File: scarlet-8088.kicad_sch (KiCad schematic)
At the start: 0 parts

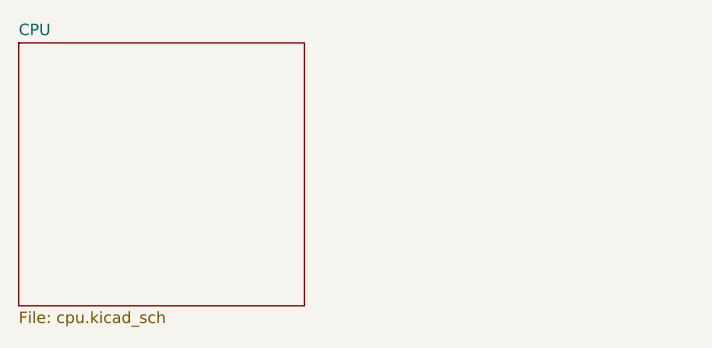
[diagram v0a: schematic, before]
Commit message: cpu and fpu connected together
Signed-off-by: Lucy Mielke <user@domain.tld>
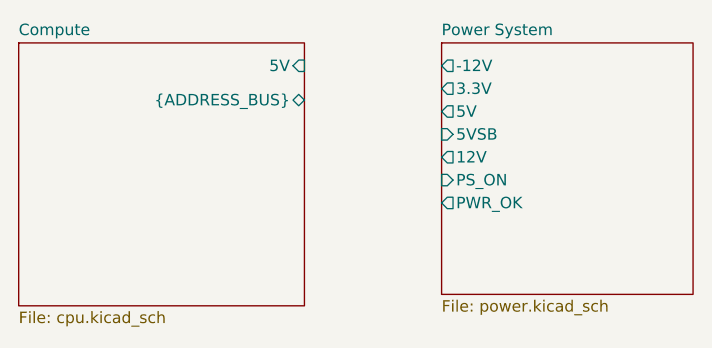
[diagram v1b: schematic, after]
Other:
- sheet CPU renamed Compute
- added sheet Power System (power.kicad_sch)
- sheet Compute ports: added 5V, {ADDRESS_BUS}; removed none
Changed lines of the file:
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@@
+	)
+	(sheet
+		(at 101.6 58.42)
+		(size 27.94 27.94)
+		(exclude_from_sim no)
+		(in_bom yes)
+		(on_board yes)
+		(dnp no)
+		(fields_autoplaced yes)
+		(stroke
+			(width 0.1524)
+			(type solid)
+		)
+		(fill
+			(color 0 0 0 0)
+		)
+		(property "Sheetname" "Power System"
+			(at 101.6 57.7084 0)
+			(show_name no)
+			(do_not_autoplace no)
+			(effects
+				(font
+					(size 1.27 1.27)
+				)
+				(justify left bottom)
+			)
+		)
+		(property "Sheetfile" "power.kicad_sch"
+			(at 101.6 86.9446 0)
+			(show_name no)
+			(do_not_autoplace no)
+			(effects
+				(font
+					(size 1.27 1.27)
+				)
+				(justify left top)
+			)
+		)
+		(pin "-12V" output
+			(at 101.6 60.96 180)
+			(effects
+				(font
+					(size 1.27 1.27)
+				)
+				(justify left)
+			)
+		)
+		(pin "3.3V" output
+			(at 101.6 63.5 180)
+			(effects
+				(font
+					(size 1.27 1.27)
+				)
+				(justify left)
+			)
+		)
+		(pin "5V" output
+			(at 101.6 66.04 180)
+			(effects
+				(font
+					(size 1.27 1.27)
+				)
+				(justify left)
+			)
+		)
+		(pin "5VSB" input
+			(at 101.6 68.58 180)
+			(effects
+				(font
+					(size 1.27 1.27)
+				)
+				(justify left)
+			)
+		)
+		(pin "12V" output
+			(at 101.6 71.12 180)
+			(effects
+				(font
+					(size 1.27 1.27)
+				)
+				(justify left)
+			)
+		)
+		(pin "PS_ON" input
+			(at 101.6 73.66 180)
+			(effects
+				(font
+					(size 1.27 1.27)
+				)
+				(justify left)
+			)
+		)
+		(pin "PWR_OK" output
+			(at 101.6 76.2 180)
+			(effects
+				(font
+					(size 1.27 1.27)
+				)
+				(justify left)
+			)
+		)
+		(instances
+			(project "scarlet-8088"
+				(path "/6bf7a8bc-eb70-43f6-b16b-1b538dd0d96d"
+					(page "2")
+				)
+			)
+		)
 	)
 	(sheet
@@
 			(color 0 0 0 0)
 		)
-		(property "Sheetname" "CPU"
+		(property "Sheetname" "Compute"
 			(at 54.61 57.7084 0)
 			(show_name no)
@@
 			)
 		)
+		(pin "5V" input
+			(at 86.36 60.96 0)
+			(effects
+				(font
+					(size 1.27 1.27)
+				)
+				(justify right)
+			)
+		)
+		(pin "{ADDRESS_BUS}" bidirectional
+			(at 86.36 64.77 0)
+			(effects
+				(font
+					(size 1.27 1.27)
+				)
+				(justify right)
+			)
+		)
 		(instances
 			(project "scarlet-8088"
 				(path "/6bf7a8bc-eb70-43f6-b16b-1b538dd0d96d"
-					(page "2")
+					(page "3")
 				)
 			)

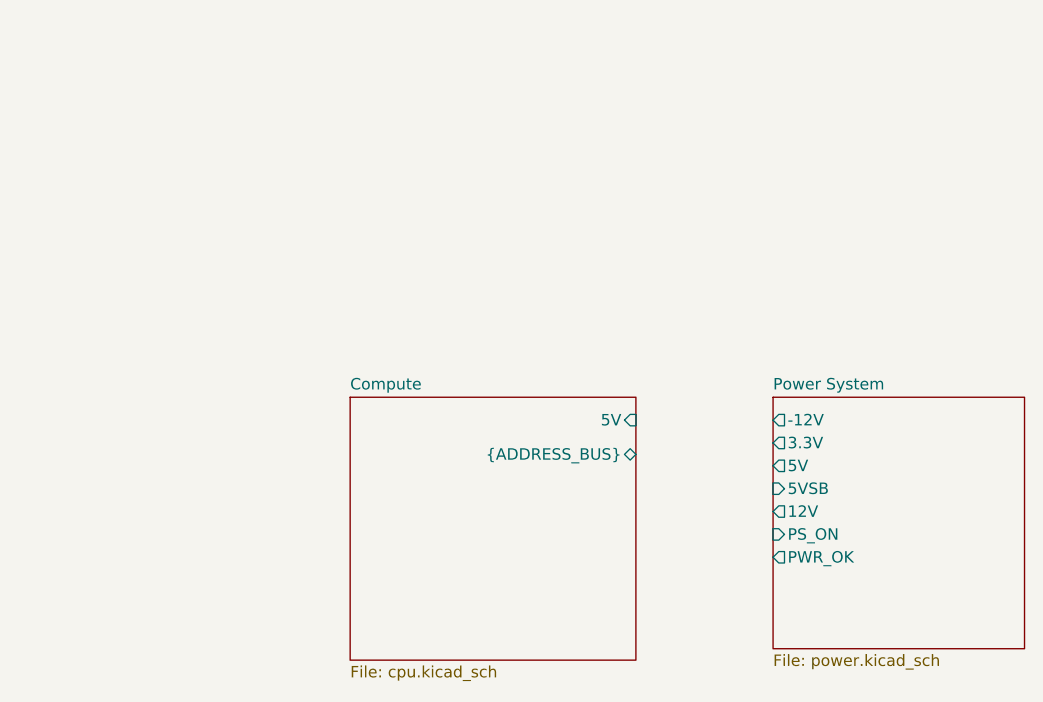
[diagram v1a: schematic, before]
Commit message: power delivery to compute basics
Signed-off-by: Lucy Mielke <user@domain.tld>
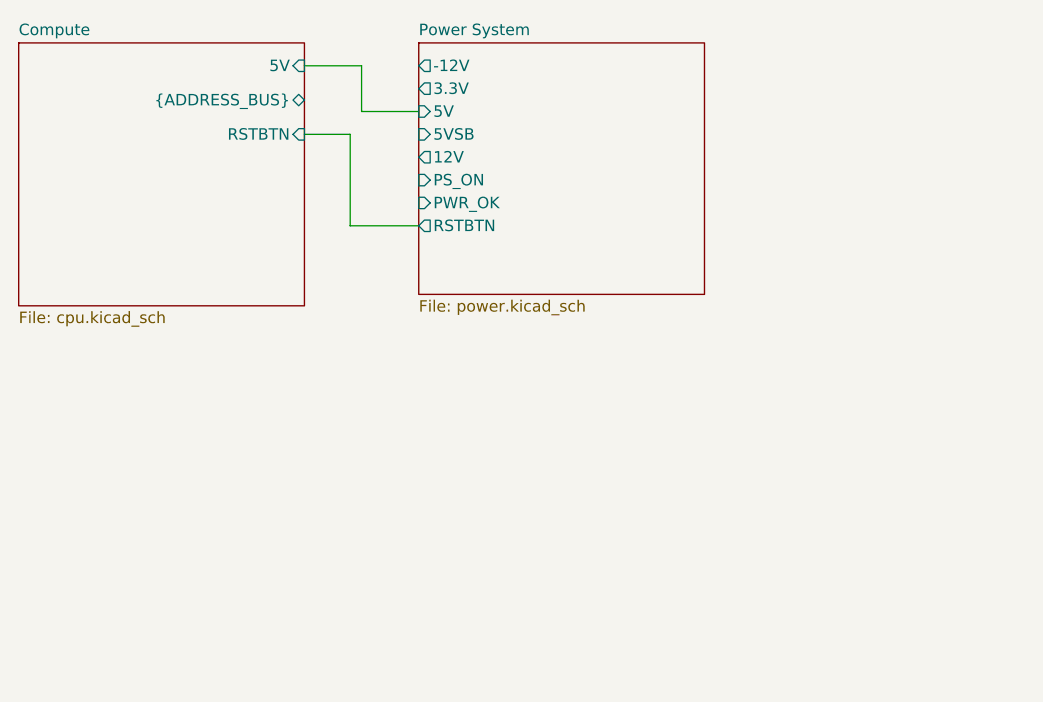
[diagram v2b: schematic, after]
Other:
- sheet Compute ports: added RSTBTN; removed none
- sheet Power System ports: added RSTBTN; removed none
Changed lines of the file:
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@@
 		(comment 1 "${COMMENT1}")
 	)
+	(wire
+		(pts
+			(xy 62.23 39.37) (xy 54.61 39.37)
+		)
+		(stroke
+			(width 0)
+			(type default)
+		)
+	)
+	(wire
+		(pts
+			(xy 62.23 26.67) (xy 55.88 26.67)
+		)
+		(stroke
+			(width 0)
+			(type default)
+		)
+	)
+	(wire
+		(pts
+			(xy 55.88 26.67) (xy 55.88 21.59)
+		)
+		(stroke
+			(width 0)
+			(type default)
+		)
+	)
+	(wire
+		(pts
+			(xy 54.61 29.21) (xy 49.53 29.21)
+		)
+		(stroke
+			(width 0)
+			(type default)
+		)
+	)
+	(wire
+		(pts
+			(xy 54.61 39.37) (xy 54.61 29.21)
+		)
+		(stroke
+			(width 0)
+			(type default)
+		)
+	)
+	(wire
+		(pts
+			(xy 55.88 21.59) (xy 49.53 21.59)
+		)
+		(stroke
+			(width 0)
+			(type default)
+		)
+	)
 	(sheet
-		(at 101.6 58.42)
-		(size 27.94 27.94)
+		(at 62.23 19.05)
+		(size 31.75 27.94)
 		(exclude_from_sim no)
 		(in_bom yes)
@@
 		)
 		(property "Sheetname" "Power System"
-			(at 101.6 57.7084 0)
+			(at 62.23 18.3384 0)
 			(show_name no)
 			(do_not_autoplace no)
@@
 		)
 		(property "Sheetfile" "power.kicad_sch"
-			(at 101.6 86.9446 0)
+			(at 62.23 47.5746 0)
 			(show_name no)
 			(do_not_autoplace no)
@@
 		)
 		(pin "-12V" output
-			(at 101.6 60.96 180)
+			(at 62.23 21.59 180)
 			(effects
 				(font
@@
 		)
 		(pin "3.3V" output
-			(at 101.6 63.5 180)
-			(effects
-				(font
-					(size 1.27 1.27)
-				)
-				(justify left)
-			)
-		)
-		(pin "5V" output
-			(at 101.6 66.04 180)
+			(at 62.23 24.13 180)
+			(effects
+				(font
+					(size 1.27 1.27)
+				)
+				(justify left)
+			)
+		)
+		(pin "5V" input
+			(at 62.23 26.67 180)
 			(effects
 				(font
@@
 		)
 		(pin "5VSB" input
-			(at 101.6 68.58 180)
+			(at 62.23 29.21 180)
 			(effects
 				(font
@@
 		)
 		(pin "12V" output
-			(at 101.6 71.12 180)
+			(at 62.23 31.75 180)
 			(effects
 				(font
@@
 		)
 		(pin "PS_ON" input
-			(at 101.6 73.66 180)
-			(effects
-				(font
-					(size 1.27 1.27)
-				)
-				(justify left)
-			)
-		)
-		(pin "PWR_OK" output
-			(at 101.6 76.2 180)
+			(at 62.23 34.29 180)
+			(effects
+				(font
+					(size 1.27 1.27)
+				)
+				(justify left)
+			)
+		)
+		(pin "PWR_OK" input
+			(at 62.23 36.83 180)
+			(effects
+				(font
+					(size 1.27 1.27)
+				)
+				(justify left)
+			)
+		)
+		(pin "RSTBTN" output
+			(at 62.23 39.37 180)
 			(effects
 				(font
@@
 	)
 	(sheet
-		(at 54.61 58.42)
+		(at 17.78 19.05)
 		(size 31.75 29.21)
 		(exclude_from_sim no)
@@
 		)
 		(property "Sheetname" "Compute"
-			(at 54.61 57.7084 0)
+			(at 17.78 18.3384 0)
 			(show_name no)
 			(do_not_autoplace no)
@@
 		)
 		(property "Sheetfile" "cpu.kicad_sch"
-			(at 54.61 88.2146 0)
+			(at 17.78 48.8446 0)
 			(show_name no)
 			(do_not_autoplace no)
@@
 		)
 		(pin "5V" input
-			(at 86.36 60.96 0)
+			(at 49.53 21.59 0)
 			(effects
 				(font
@@
 		)
 		(pin "{ADDRESS_BUS}" bidirectional
-			(at 86.36 64.77 0)
-			(effects
-				(font
+			(at 49.53 25.4 0)
+			(effects
+				(font
+					(size 1.27 1.27)
+				)
+				(justify right)
+			)
+		)
+		(pin "RSTBTN" input
+			(at 49.53 29.21 0)
+			(effects
+				(font

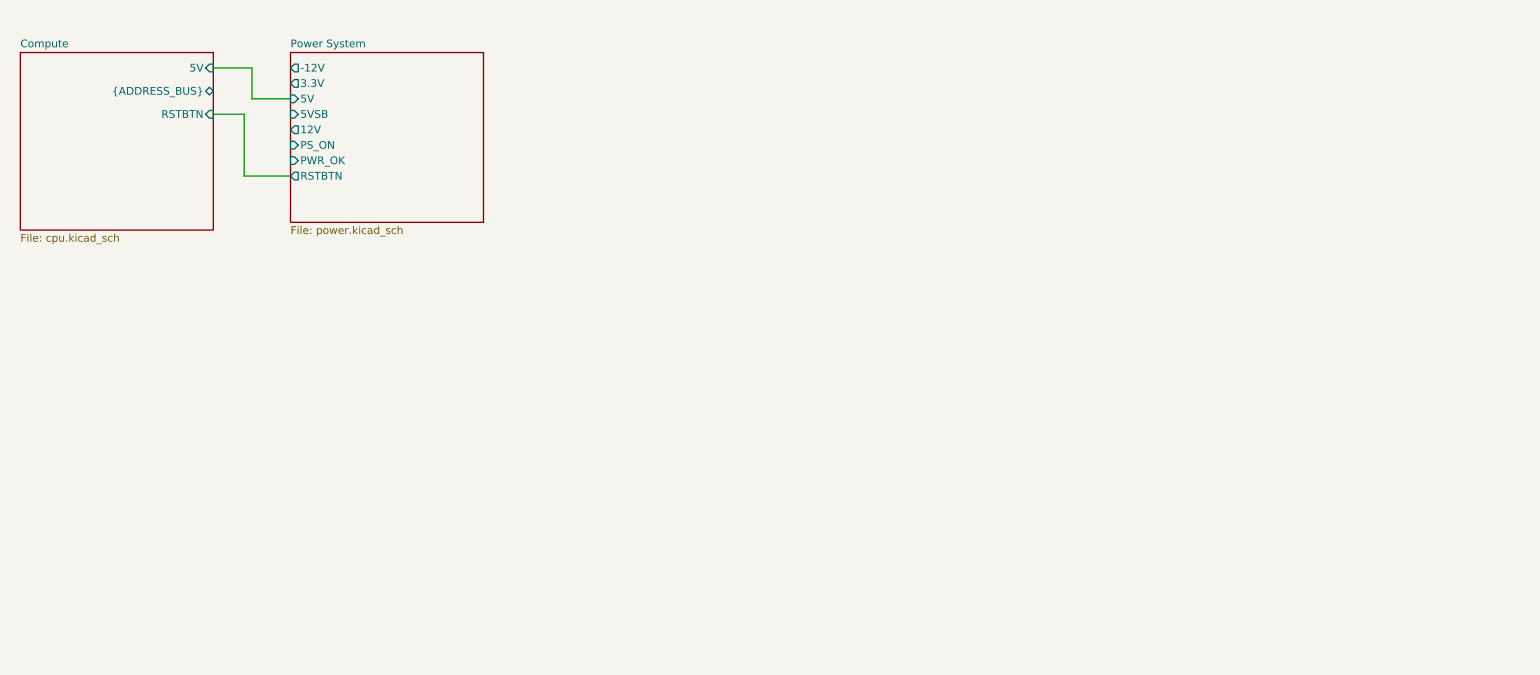
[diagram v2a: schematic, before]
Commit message: Add grounded Mounting Holes to schematic
Signed-off-by: Lucy Mielke <user@domain.tld>
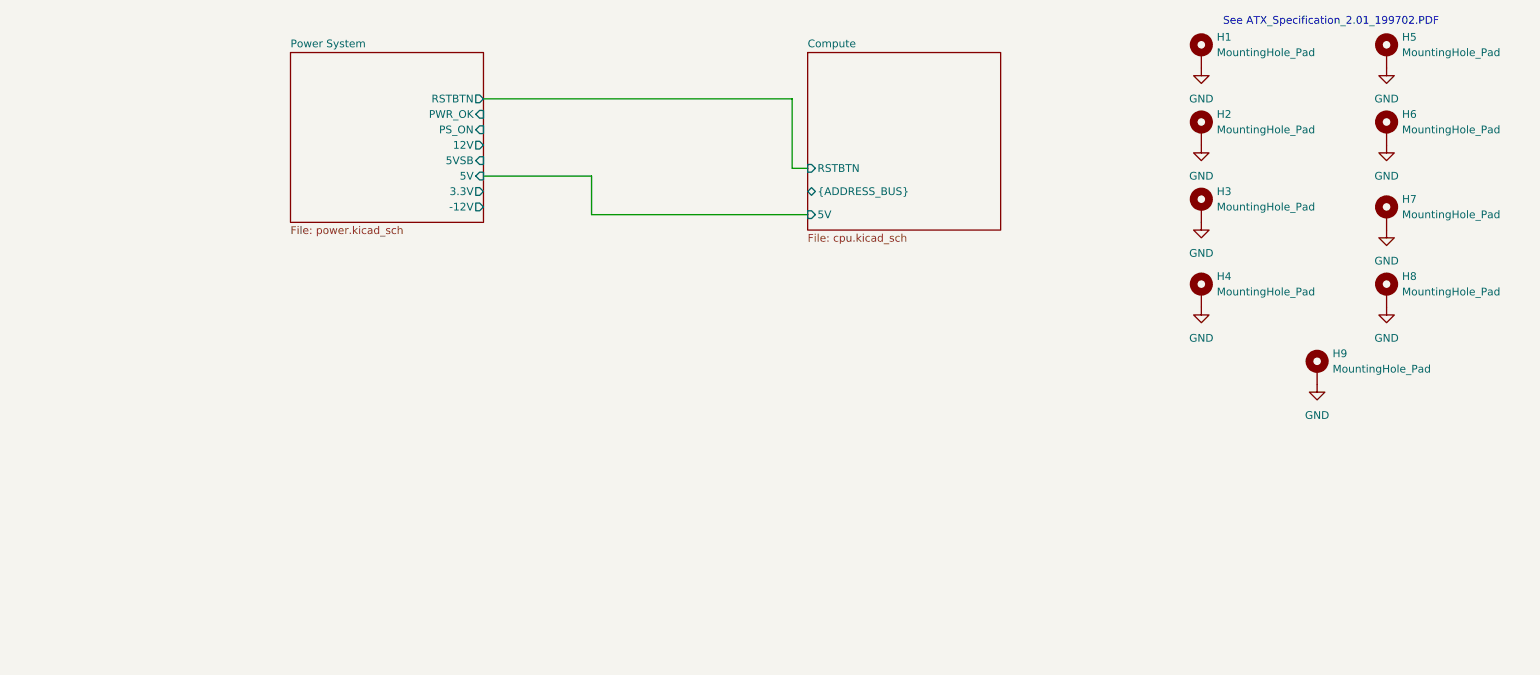
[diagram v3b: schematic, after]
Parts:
- added H1, H2, H3, H4, H5, H6, H7, H8, H9: MountingHole_Pad, MountingHole:MountingHole_3.2mm_M3_Pad_TopBottom, symbol Mechanical:MountingHole_Pad
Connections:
- new net GND: H1.1, H2.1, H3.1, H4.1, H5.1, H6.1, H7.1, H8.1, H9.1
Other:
- note added: "See ATX_Specification_2.01_199702.PDF"

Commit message: Memory mapping for RAM and ROM (BIOS)
Signed-off-by: Lucy Mielke <user@domain.tld>
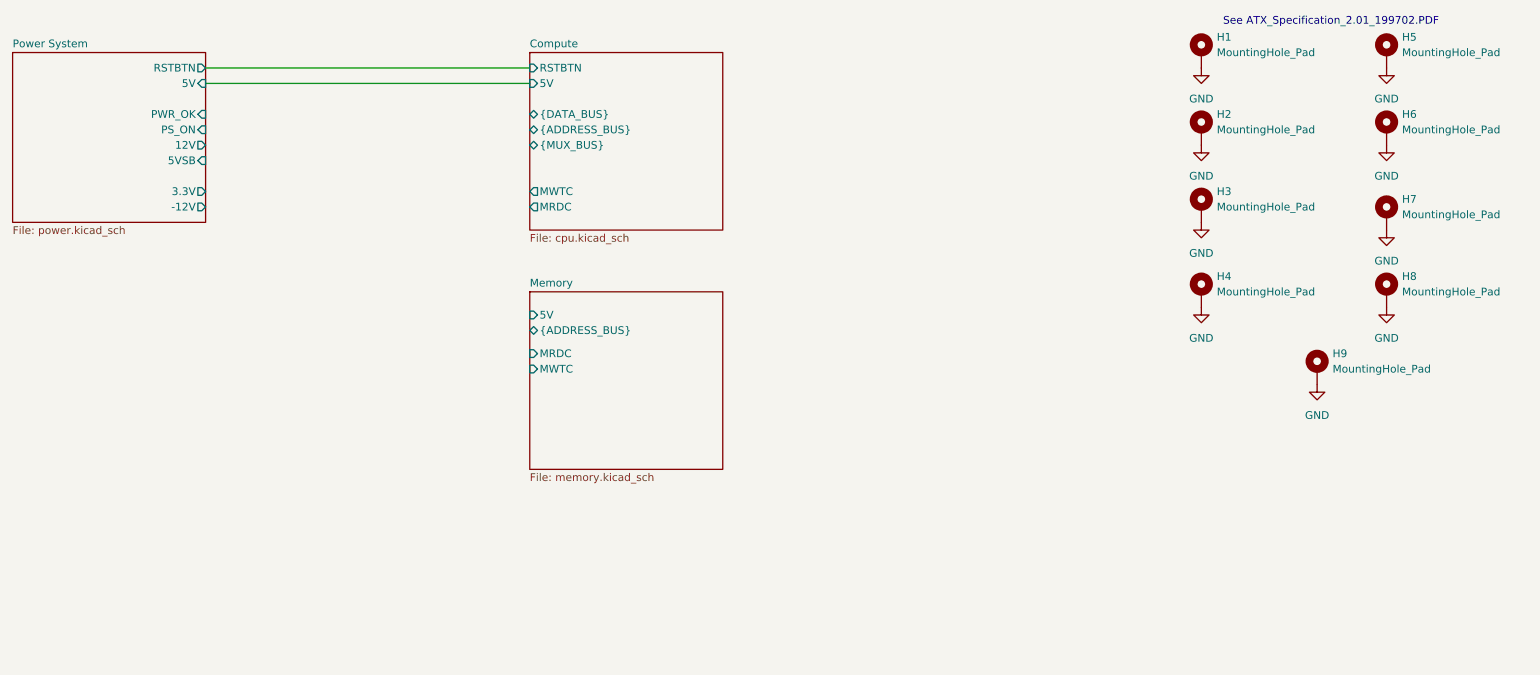
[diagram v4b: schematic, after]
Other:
- added sheet Memory (memory.kicad_sch)
- sheet Compute ports: added MRDC, MWTC, {DATA_BUS}, {MUX_BUS}; removed none
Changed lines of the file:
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@@
 	(wire
 		(pts
-			(xy 93.98 26.67) (xy 144.78 26.67)
+			(xy 48.26 21.59) (xy 101.6 21.59)
 		)
 		(stroke
@@
 	(wire
 		(pts
-			(xy 144.78 38.1) (xy 147.32 38.1)
+			(xy 48.26 24.13) (xy 101.6 24.13)
 		)
 		(stroke
@@
 		)
 	)
-	(wire
-		(pts
-			(xy 111.76 45.72) (xy 111.76 39.37)
-		)
-		(stroke
-			(width 0)
-			(type default)
-		)
-	)
-	(wire
-		(pts
-			(xy 144.78 26.67) (xy 144.78 38.1)
-		)
-		(stroke
-			(width 0)
-			(type default)
-		)
-	)
-	(wire
-		(pts
-			(xy 111.76 39.37) (xy 93.98 39.37)
-		)
-		(stroke
-			(width 0)
-			(type default)
-		)
-	)
-	(wire
-		(pts
-			(xy 147.32 45.72) (xy 111.76 45.72)
-		)
-		(stroke
-			(width 0)
-			(type default)
-		)
-	)
 	(symbol
 		(lib_id "Mechanical:MountingHole_Pad")
@@
 	)
 	(sheet
-		(at 62.23 19.05)
+		(at 16.51 19.05)
 		(size 31.75 27.94)
 		(exclude_from_sim no)
@@
 		)
 		(property "Sheetname" "Power System"
-			(at 62.23 18.3384 0)
+			(at 16.51 18.3384 0)
 			(show_name no)
 			(do_not_autoplace no)
@@
 		)
 		(property "Sheetfile" "power.kicad_sch"
-			(at 62.23 47.5746 0)
+			(at 16.51 47.5746 0)
 			(show_name no)
 			(do_not_autoplace no)
@@
 		)
 		(pin "-12V" output
-			(at 93.98 44.45 0)
+			(at 48.26 44.45 0)
 			(effects
 				(font
@@
 		)
 		(pin "3.3V" output
-			(at 93.98 41.91 0)
+			(at 48.26 41.91 0)
 			(effects
 				(font
@@
 		)
 		(pin "5V" input
-			(at 93.98 39.37 0)
+			(at 48.26 24.13 0)
 			(effects
 				(font
@@
 		)
 		(pin "5VSB" input
-			(at 93.98 36.83 0)
+			(at 48.26 36.83 0)
 			(effects
 				(font
@@
 		)
 		(pin "12V" output
-			(at 93.98 34.29 0)
+			(at 48.26 34.29 0)
 			(effects
 				(font
@@
 		)
 		(pin "PS_ON" input
-			(at 93.98 31.75 0)
+			(at 48.26 31.75 0)
 			(effects
 				(font
@@
 		)
 		(pin "PWR_OK" input
-			(at 93.98 29.21 0)
+			(at 48.26 29.21 0)
 			(effects
 				(font
@@
 		)
 		(pin "RSTBTN" output
-			(at 93.98 26.67 0)
+			(at 48.26 21.59 0)
 			(effects
 				(font
@@
 	)
 	(sheet
-		(at 147.32 19.05)
+		(at 101.6 58.42)
 		(size 31.75 29.21)
 		(exclude_from_sim no)
@@
 			(color 0 0 0 0)
 		)
+		(property "Sheetname" "Memory"
+			(at 101.6 57.7084 0)
+			(show_name no)
+			(do_not_autoplace no)
+			(effects
+				(font
+					(size 1.27 1.27)
+				)
+				(justify left bottom)
+			)
+		)
+		(property "Sheetfile" "memory.kicad_sch"
+			(at 101.6 88.2146 0)
+			(show_name no)
+			(do_not_autoplace no)
+			(effects
+				(font
+					(size 1.27 1.27)
+				)
+				(justify left top)
+			)
+		)
+		(pin "5V" input
+			(at 101.6 62.23 180)
+			(effects
+				(font
+					(size 1.27 1.27)
+				)
+				(justify left)
+			)
+		)
+		(pin "{ADDRESS_BUS}" bidirectional
+			(at 101.6 64.77 180)
+			(effects
+				(font
+					(size 1.27 1.27)
+				)
+				(justify left)
+			)
+		)
+		(pin "MRDC" input
+			(at 101.6 68.58 180)
+			(effects
+				(font
+					(size 1.27 1.27)
+				)
+				(justify left)
+			)
+		)
+		(pin "MWTC" input
+			(at 101.6 71.12 180)
+			(effects
+				(font
+					(size 1.27 1.27)
+				)
+				(justify left)
+			)
+		)
+		(instances
+			(project "scarlet-8088"
+				(path "/6bf7a8bc-eb70-43f6-b16b-1b538dd0d96d"
+					(page "4")
+				)
+			)
+		)
+	)
+	(sheet
+		(at 101.6 19.05)
+		(size 31.75 29.21)
+		(exclude_from_sim no)
+		(in_bom yes)
+		(on_board yes)
+		(dnp no)
+		(fields_autoplaced yes)
+		(stroke
+			(width 0.1524)
+			(type solid)
+		)
+		(fill
+			(color 0 0 0 0)
+		)
 		(property "Sheetname" "Compute"
-			(at 147.32 18.3384 0)
+			(at 101.6 18.3384 0)
 			(show_name no)
 			(do_not_autoplace no)
@@
 		)
 		(property "Sheetfile" "cpu.kicad_sch"
-			(at 147.32 48.8446 0)
+			(at 101.6 48.8446 0)
 			(show_name no)
 			(do_not_autoplace no)
@@
 		)
 		(pin "5V" input
-			(at 147.32 45.72 180)
+			(at 101.6 24.13 180)
 			(effects
 				(font
@@
 		)
 		(pin "{ADDRESS_BUS}" bidirectional
-			(at 147.32 41.91 180)
+			(at 101.6 31.75 180)
 			(effects
 				(font
@@
 		)
 		(pin "RSTBTN" input
-			(at 147.32 38.1 180)
-			(effects
-				(font
+			(at 101.6 21.59 180)
+			(effects
+				(font
+					(size 1.27 1.27)
+				)
+				(justify left)
+			)
+		)
+		(pin "MRDC" output
+			(at 101.6 44.45 180)
+			(effects
+				(font
+					(size 1.27 1.27)
+				)
+				(justify left)
+			)
+		)
+		(pin "MWTC" output
+			(at 101.6 41.91 180)
+			(effects
+				(font
+					(size 1.27 1.27)
+				)
+				(justify left)
+			)
+		)
+		(pin "{DATA_BUS}" bidirectional
+			(at 101.6 29.21 180)
+			(effects
+				(font
+					(size 1.27 1.27)
+				)
+				(justify left)
+			)
+		)
+		(pin "{MUX_BUS}" bidirectional
+			(at 101.6 34.29 180)
+			(effects
+				(font
